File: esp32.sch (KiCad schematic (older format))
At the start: 4 parts, among them IC1 ESP32-WROVER-E_M213EH6464PH3Q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, J2 Conn_01x10_Male, J3 Conn_01x10_Male

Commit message: EN Pullup, DTR + RTS
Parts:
- added C6: 100nF, Capacitor_SMD:C_0603_1608Metric, symbol Device:C
- added Q1: UMH3N, Package_TO_SOT_SMD:SOT-363_SC-70-6, symbol Transistor_BJT:UMH3N
- added R7: 10k, Resistor_SMD:R_0603_1608Metric, symbol Device:R
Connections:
- net labels added: DTR, EN, IO0, RTS, RXD, TXD
- wire segments 56 -> 53
- no-connect marks 13 -> 12
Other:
- moved on the sheet: IC1

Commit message: Alle ESP Pins
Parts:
- removed Q1: UMH3N, Package_TO_SOT_SMD:SOT-363_SC-70-6, symbol Transistor_BJT:UMH3N
- J2: value Conn_01x10_Male -> Conn_01x14_Male; footprint Connector_PinHeader_2.54mm:PinHeader_1x10_P2.54mm_Vertical -> Connector_PinHeader_2.54mm:PinHeader_1x14_P2.54mm_Vertical; symbol Connector:Conn_01x10_Male -> Connector:Conn_01x14_Male
- J3: value Conn_01x10_Male -> Conn_01x16_Male; footprint Connector_PinHeader_2.54mm:PinHeader_1x10_P2.54mm_Vertical -> Connector_PinHeader_2.54mm:PinHeader_1x16_P2.54mm_Vertical; symbol Connector:Conn_01x10_Male -> Connector:Conn_01x16_Male
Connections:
- net labels removed: DTR, RTS
- wire segments 53 -> 58
- no-connect marks 12 -> 11
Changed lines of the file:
@@
 $EndSheet
 $Comp
-L Connector:Conn_01x10_Male J2
+L Connector:Conn_01x14_Male J2
 U 1 1 60ED5AC0
-P 1450 5350
-F 0 "J2" H 1050 5350 50  0000 C CNN
-F 1 "Conn_01x10_Male" H 1100 5250 50  0000 C CNN
-F 2 "Connector_PinHeader_2.54mm:PinHeader_1x10_P2.54mm_Vertical" H 1450 5350 50  0001 C CNN
-F 3 "~" H 1450 5350 50  0001 C CNN
-	1    1450 5350
-	1    0    0    -1
-$EndComp
-$Comp
-L Connector:Conn_01x10_Male J3
-U 1 1 60ED67E8
-P 5400 5650
-F 0 "J3" H 5372 5532 50  0000 R CNN
-F 1 "Conn_01x10_Male" H 5372 5623 50  0000 R CNN
-F 2 "Connector_PinHeader_2.54mm:PinHeader_1x10_P2.54mm_Vertical" H 5400 5650 50  0001 C CNN
-F 3 "~" H 5400 5650 50  0001 C CNN
-	1    5400 5650
-	-1   0    0    1
+P 1450 5550
+F 0 "J2" H 1050 5550 50  0000 C CNN
+F 1 "Conn_01x14_Male" H 1100 5450 50  0000 C CNN
+F 2 "Connector_PinHeader_2.54mm:PinHeader_1x14_P2.54mm_Vertical" H 1450 5550 50  0001 C CNN
+F 3 "~" H 1450 5550 50  0001 C CNN
+	1    1450 5550
+	1    0    0    -1
 $EndComp
 Wire Wire Line
@@
 L power:GND #PWR0119
 U 1 1 60EF68BA
-P 2000 7050
-F 0 "#PWR0119" H 2000 6800 50  0001 C CNN
-F 1 "GND" H 2005 6877 50  0000 C CNN
-F 2 "" H 2000 7050 50  0001 C CNN
-F 3 "" H 2000 7050 50  0001 C CNN
-	1    2000 7050
-	1    0    0    -1
-$EndComp
-Wire Wire Line
-	2600 6250 2000 6250
-Wire Wire Line
-	2000 6250 2000 7050
+P 2150 7050
+F 0 "#PWR0119" H 2150 6800 50  0001 C CNN
+F 1 "GND" H 2155 6877 50  0000 C CNN
+F 2 "" H 2150 7050 50  0001 C CNN
+F 3 "" H 2150 7050 50  0001 C CNN
+	1    2150 7050
+	1    0    0    -1
+$EndComp
+Wire Wire Line
+	2600 6250 2150 6250
+Wire Wire Line
+	2150 6250 2150 7050
 NoConn ~ 4100 5150
 NoConn ~ 4100 5550
@@
 	4100 7050 4500 7050
 Connection ~ 4500 7050
-NoConn ~ 2600 5150
-NoConn ~ 2600 5250
-Text GLabel 5150 5150 0    50   Input ~ 0
+Text GLabel 5100 4650 0    50   Input ~ 0
 CANH
-Text GLabel 5150 5250 0    50   Input ~ 0
+Text GLabel 5100 4750 0    50   Input ~ 0
 CANL
-Wire Wire Line
-	4100 5650 5200 5650
-Wire Wire Line
-	4100 5250 4650 5250
-Wire Wire Line
-	4650 5250 4650 5550
-Wire Wire Line
-	4650 5550 5200 5550
-Wire Wire Line
-	4100 4950 4750 4950
-Wire Wire Line
-	4750 4950 4750 5450
-Wire Wire Line
-	4750 5450 5200 5450
 NoConn ~ 4100 5050
 $Comp
 L power:GND #PWR0118
 U 1 1 60F7017A
-P 5200 6050
-F 0 "#PWR0118" H 5200 5800 50  0001 C CNN
-F 1 "GND" H 5205 5877 50  0000 C CNN
-F 2 "" H 5200 6050 50  0001 C CNN
-F 3 "" H 5200 6050 50  0001 C CNN
-	1    5200 6050
-	1    0    0    -1
-$EndComp
-Text GLabel 2600 5050 0    50   Input ~ 0
-EN
-Text GLabel 1700 5050 2    50   Input ~ 0
-EN
-Text GLabel 5150 5350 0    50   Input ~ 0
+P 5200 6150
+F 0 "#PWR0118" H 5200 5900 50  0001 C CNN
+F 1 "GND" H 5205 5977 50  0000 C CNN
+F 2 "" H 5200 6150 50  0001 C CNN
+F 3 "" H 5200 6150 50  0001 C CNN
+	1    5200 6150
+	1    0    0    -1
+$EndComp
+Text GLabel 5100 5150 0    50   Input ~ 0
 IO0
 Text GLabel 4100 4850 2    50   Input ~ 0
@@
 	1    0    0    -1
 $EndComp
-$Comp
-L Transistor_BJT:UMH3N Q1
-U 1 1 60EB7CC3
-P 2950 3500
-F 0 "Q1" H 3240 3546 50  0000 L CNN
-F 1 "UMH3N" H 3240 3455 50  0000 L CNN
-F 2 "Package_TO_SOT_SMD:SOT-363_SC-70-6" H 2955 3060 50  0001 C CNN
-F 3 "http://rohmfs.rohm.com/en/products/databook/datasheet/discrete/transistor/digital/emh3t2r-e.pdf" H 3100 3500 50  0001 C CNN
-	1    2950 3500
-	1    0    0    -1
-$EndComp
-Text GLabel 3150 3300 1    50   Input ~ 0
-EN
-Text GLabel 2750 3500 0    50   Input ~ 0
-DTR
-Text GLabel 3150 3700 3    50   Input ~ 0
-RTS
-$Comp
-L Transistor_BJT:UMH3N Q1
-U 2 1 60EB8B73
-P 4000 3500
-F 0 "Q1" H 4290 3546 50  0000 L CNN
-F 1 "UMH3N" H 4290 3455 50  0000 L CNN
-F 2 "Package_TO_SOT_SMD:SOT-363_SC-70-6" H 4005 3060 50  0001 C CNN
-F 3 "http://rohmfs.rohm.com/en/products/databook/datasheet/discrete/transistor/digital/emh3t2r-e.pdf" H 4150 3500 50  0001 C CNN
-	2    4000 3500
-	1    0    0    -1
-$EndComp
-Text GLabel 4200 3300 1    50   Input ~ 0
-IO0
-Text GLabel 4200 3700 3    50   Input ~ 0
-DTR
-Text GLabel 3800 3500 0    50   Input ~ 0
-RTS
-Text GLabel 5150 5750 0    50   Input ~ 0
+Text GLabel 5100 5750 0    50   Input ~ 0
 RXD
-Text GLabel 5150 5850 0    50   Input ~ 0
+Text GLabel 5100 5850 0    50   Input ~ 0
 TXD
-Text GLabel 1700 5150 2    50   Input ~ 0
-DTR
-Text GLabel 1700 5250 2    50   Input ~ 0
-RTS
 $Comp
 L power:GND #PWR0122
@@
 TXD
 Wire Wire Line
-	2600 5950 2000 5950
-Wire Wire Line
-	2000 5950 2000 5750
-Wire Wire Line
-	2000 5750 1650 5750
-Wire Wire Line
-	4100 5950 5200 5950
-Wire Wire Line
-	1650 5850 1900 5850
-Wire Wire Line
-	1900 5850 1900 6150
-Wire Wire Line
-	1900 6150 2600 6150
-Wire Wire Line
 	1650 4950 1750 4950
-Wire Wire Line
-	1650 5050 1700 5050
-Wire Wire Line
-	1650 5150 1700 5150
-Wire Wire Line
-	1650 5250 1700 5250
-Wire Wire Line
-	5150 5150 5200 5150
-Wire Wire Line
-	5150 5250 5200 5250
-Wire Wire Line
-	5150 5350 5200 5350
-Wire Wire Line
-	5150 5750 5200 5750
-Wire Wire Line
-	5150 5850 5200 5850
-$Comp
-L power:+3.3V #PWR?
+$Comp
+L power:+3.3V #PWR0123
 U 1 1 60F07F5A
 P 1750 4850
-F 0 "#PWR?" H 1750 4700 50  0001 C CNN
+F 0 "#PWR0123" H 1750 4700 50  0001 C CNN
 F 1 "+3.3V" H 1765 5023 50  0000 C CNN
 F 2 "" H 1750 4850 50  0001 C CNN
@@
 Wire Wire Line
 	1750 4950 2600 4950
+$Comp
+L Connector:Conn_01x16_Male J3
+U 1 1 60ED67E8
+P 5400 5450
+F 0 "J3" H 5372 5332 50  0000 R CNN
+F 1 "Conn_01x16_Male" H 5372 5423 50  0000 R CNN
+F 2 "Connector_PinHeader_2.54mm:PinHeader_1x16_P2.54mm_Vertical" H 5400 5450 50  0001 C CNN
+F 3 "~" H 5400 5450 50  0001 C CNN
+	1    5400 5450
+	-1   0    0    1
+$EndComp
+Text GLabel 5100 6050 0    50   Input ~ 0
+MCP_MOSI
+Text GLabel 5100 5550 0    50   Input ~ 0
+MCP_MISO
+Text GLabel 5100 5450 0    50   Input ~ 0
+MCP_CLK
+Wire Wire Line
+	5100 6050 5200 6050
+Wire Wire Line
+	4100 5950 5200 5950
+Wire Wire Line
+	5100 5850 5200 5850
+Wire Wire Line
+	5100 5750 5200 5750
+Wire Wire Line
+	4100 5650 5200 5650
+Wire Wire Line
+	4600 5250 4600 5350
+Wire Wire Line
+	4600 5350 5200 5350
+Wire Wire Line
+	4100 5250 4600 5250
+Wire Wire Line
+	4100 4950 4700 4950
+Wire Wire Line
+	4700 4950 4700 5250
+Wire Wire Line
+	4700 5250 5200 5250
+Wire Wire Line
+	5100 5150 5200 5150
+Text GLabel 5100 5050 0    50   Input ~ 0
+SD_DAT0
+Text GLabel 5100 4950 0    50   Input ~ 0
+SD_CMD
+Wire Wire Line
+	1650 5150 2600 5150
+Wire Wire Line
+	1650 5250 2600 5250
+Text GLabel 1750 5750 2    50   Input ~ 0
+MCP_CS
+Text GLabel 1750 5850 2    50   Input ~ 0
+MCP_INT
+Text GLabel 1750 6050 2    50   Input ~ 0
+SD_CLK
+Text GLabel 1750 6250 2    50   Input ~ 0
+SD_DAT3
+Wire Wire Line
+	1650 5750 1750 5750
+Wire Wire Line
+	1650 5850 1750 5850
+Wire Wire Line
+	1650 5950 2600 5950
+Wire Wire Line
+	1650 6050 1750 6050
+Wire Wire Line
+	1650 6250 1750 6250
+Wire Wire Line
+	1650 6150 2600 6150
+Wire Wire Line
+	5100 4650 5200 4650
+Wire Wire Line
+	5100 4750 5200 4750
+Wire Wire Line
+	5100 4950 5200 4950
+Wire Wire Line
+	5100 5050 5200 5050
+Wire Wire Line
+	5100 5450 5200 5450
+Wire Wire Line
+	5100 5550 5200 5550
+Text GLabel 2600 5050 0    50   Input ~ 0
+EN
+Text GLabel 1750 5050 2    50   Input ~ 0
+EN
+Wire Wire Line
+	1650 5050 1750 5050
+NoConn ~ 5200 4850
 $EndSCHEMATC

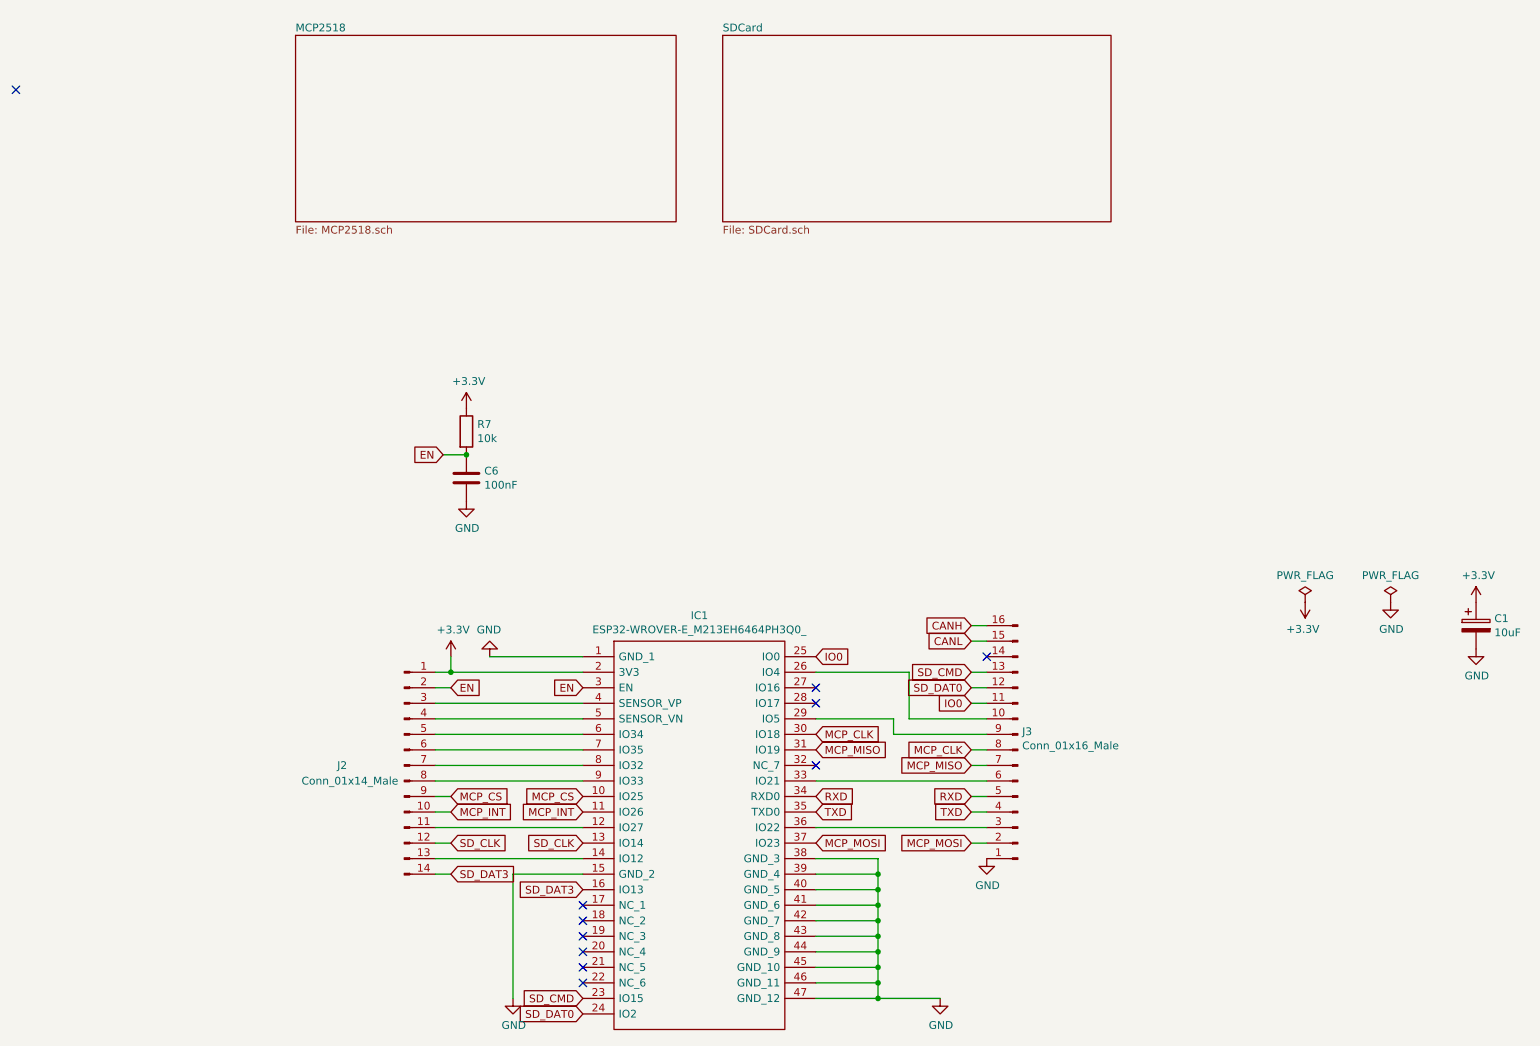
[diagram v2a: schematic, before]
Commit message: ESP32 Bus extrahiert
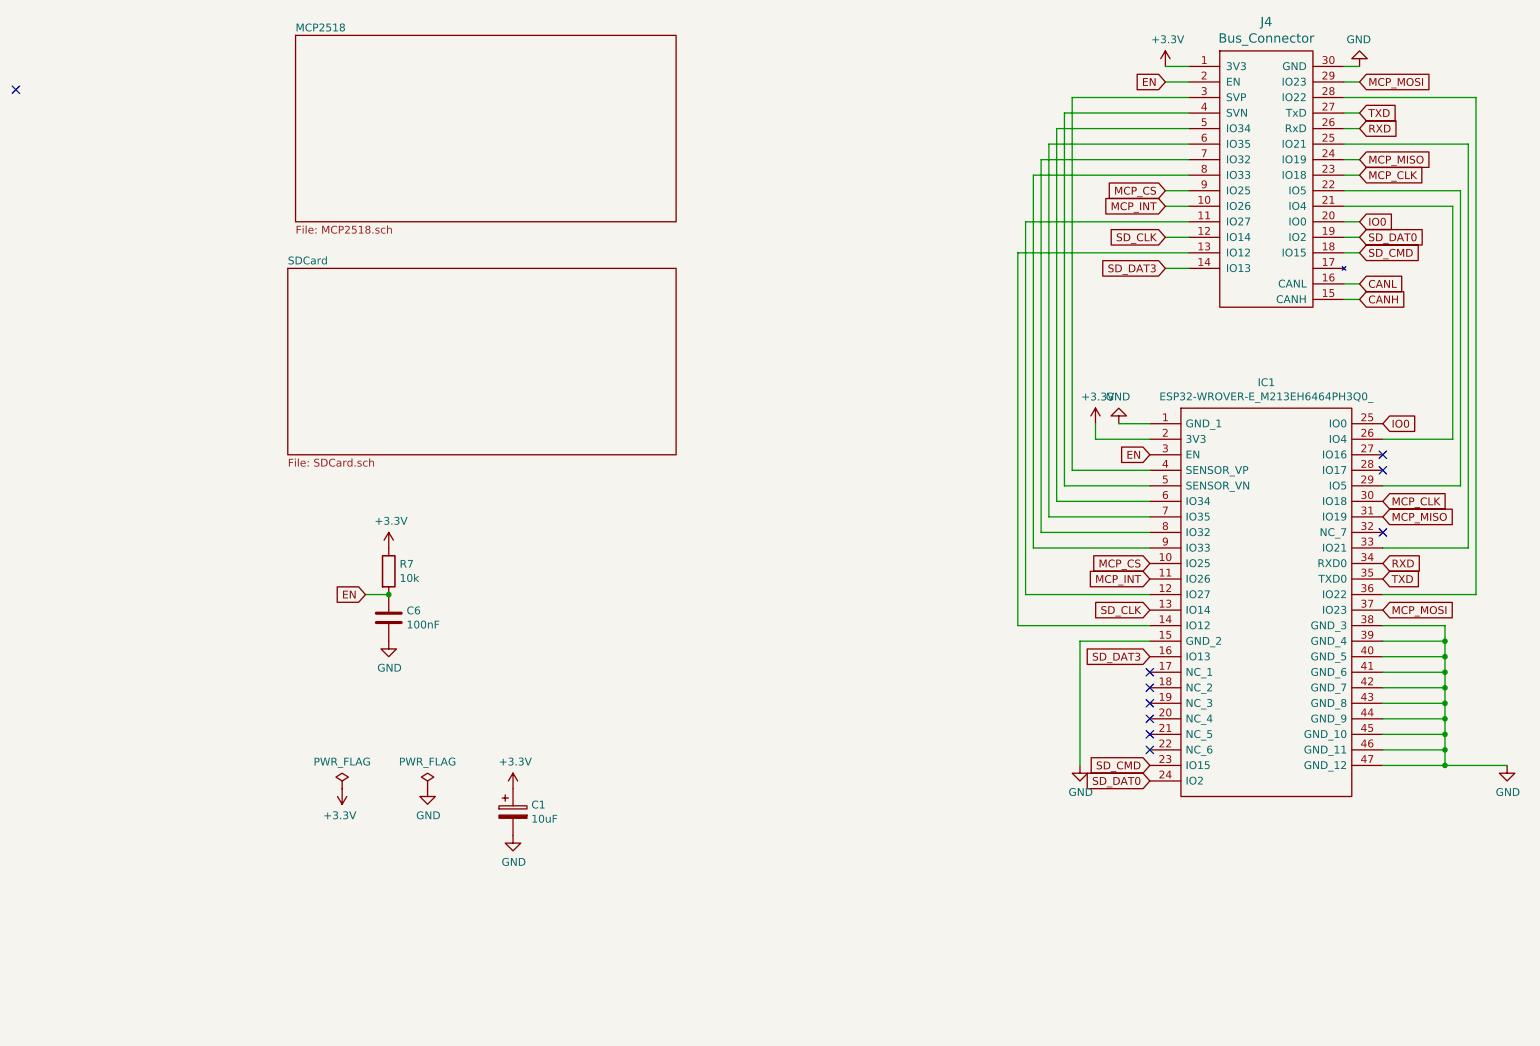
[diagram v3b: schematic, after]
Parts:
- removed J2: Conn_01x14_Male, Connector_PinHeader_2.54mm:PinHeader_1x14_P2.54mm_Vertical, symbol Connector:Conn_01x14_Male
- removed J3: Conn_01x16_Male, Connector_PinHeader_2.54mm:PinHeader_1x16_P2.54mm_Vertical, symbol Connector:Conn_01x16_Male
- added J4: Bus_Connector, esp32bus:PinHeader, symbol ESP32_Bus:Bus_Connector
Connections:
- net +3V3: now also J4.1 (3V3)
- net CANH: now also J4.15 (CANH)
- net CANL: now also J4.16 (CANL)
- net EN: now also J4.2 (EN)
- net GND: now also J4.30 (GND)
- net IO0: now also J4.20 (IO0)
- net MCP_CLK: now also J4.23 (IO18)
- net MCP_CS: now also J4.9 (IO25)
- net MCP_INT: now also J4.10 (IO26)
- net MCP_MISO: now also J4.24 (IO19)
- net MCP_MOSI: now also J4.29 (IO23)
- net RXD: now also J4.26 (RxD)
- net SD_CLK: now also J4.12 (IO14)
- net SD_CMD: now also J4.18 (IO15)
- net SD_DAT0: now also J4.19 (IO2)
- net SD_DAT3: now also J4.14 (IO13)
- net TXD: now also J4.27 (TxD)
- net at IC1.12 (IO27): now also J4.11 (IO27)
- net at IC1.14 (IO12): now also J4.13 (IO12)
- net at IC1.26 (IO4): now also J4.21 (IO4)
- net at IC1.29 (IO5): now also J4.22 (IO5)
- net at IC1.33 (IO21): now also J4.25 (IO21)
- net at IC1.36 (IO22): now also J4.28 (IO22)
- net at IC1.4 (SENSOR_VP): now also J4.3 (SVP)
- net at IC1.5 (SENSOR_VN): now also J4.4 (SVN)
- net at IC1.6 (IO34): now also J4.5 (IO34)
- net at IC1.7 (IO35): now also J4.6 (IO35)
- net at IC1.8 (IO32): now also J4.7 (IO32)
- net at IC1.9 (IO33): now also J4.8 (IO33)
- no-connect marks 11 -> 10
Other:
- moved on the sheet: C1, C6, IC1, R7

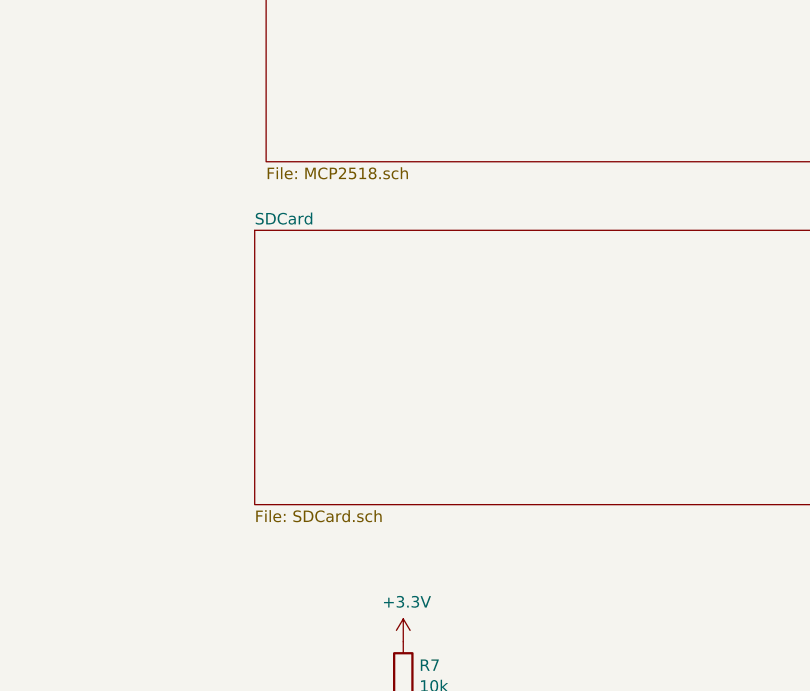
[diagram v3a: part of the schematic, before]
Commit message: SD Card und MCP extrahiert
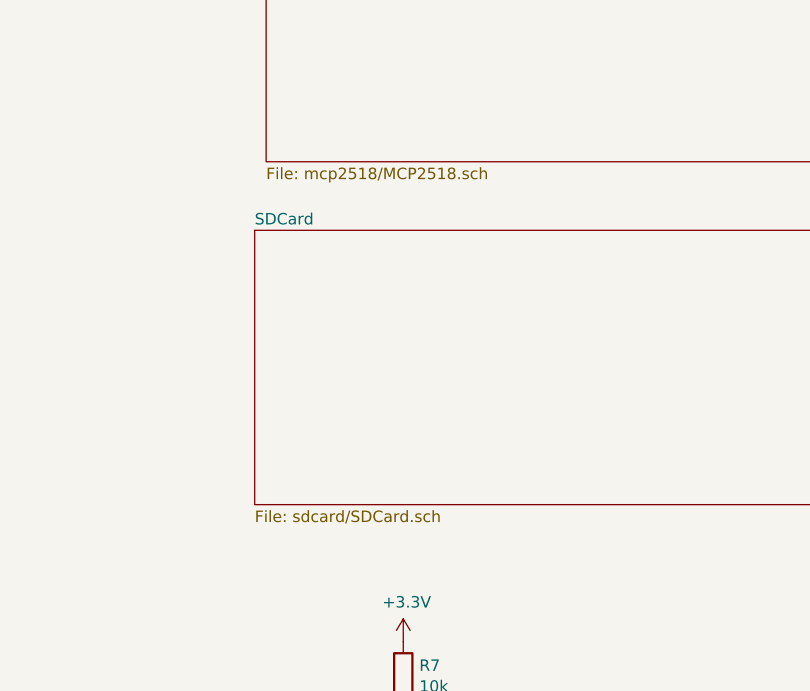
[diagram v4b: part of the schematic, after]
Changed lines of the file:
@@
 U 60EA716F
 F0 "MCP2518" 50
-F1 "MCP2518.sch" 50
+F1 "mcp2518/MCP2518.sch" 50
 $EndSheet
 $Sheet
@@
 U 60EC0178
 F0 "SDCard" 50
-F1 "SDCard.sch" 50
+F1 "sdcard/SDCard.sch" 50
 $EndSheet
 $Comp
